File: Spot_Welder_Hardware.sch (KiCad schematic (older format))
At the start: 148 parts, among them J1 Mini USB, J2 Conn_01x03_Male, Q1 Q_NMOS_GSD, Q10 Q_NMOS_GDS, Q11 Q_NMOS_GDS, Q12 Q_NMOS_GDS, Q13 Q_NMOS_GDS, Q2 MBT3904, Q3 Q_NMOS_GDS, Q4 Q_NMOS_GDS, Q5 Q_NMOS_GDS, Q6 Q_NMOS_GDS, Q7 Q_NMOS_GDS, Q8 Q_NMOS_GDS, Q9 Q_NMOS_GDS, SW1 SW_Push, SW2 SW_SPDT, SW3 Lead Voltage Trigger, SW4 SW_Push, U1 OKI, U2 ATMEGA328P, U3 FAN3122TMXCT-ND, U4 FT232RL, U5 FAN3122TMXCT-ND, Y1 Crystal

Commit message: Updated shematic libraries
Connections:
- wire segments 326 -> 328
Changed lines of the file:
@@
 L MRDT_Connectors:AndersonPP Conn3
 U 1 1 5BB3DDFC
-P 5300 4200
-F 0 "Conn3" H 5506 4587 60  0000 C CNN
-F 1 "AndersonPP" H 5506 4481 60  0000 C CNN
-F 2 "MRDT_Connectors:Anderson_2_Horisontal_Side_by_Side" H 5150 3650 60  0001 C CNN
-F 3 "" H 5150 3650 60  0001 C CNN
-	1    5300 4200
+P 5250 4200
+F 0 "Conn3" H 5456 4587 60  0001 C CNN
+F 1 "AndersonPP" H 5456 4481 60  0001 C CNN
+F 2 "MRDT_Connectors:Anderson_2_Horisontal_Side_by_Side" H 5100 3650 60  0001 C CNN
+F 3 "" H 5100 3650 60  0001 C CNN
+	1    5250 4200
 	1    0    0    -1
 $EndComp
@@
 L MRDT_Connectors:AndersonPP Conn3
 U 2 1 5BB3DF96
-P 5300 3900
-F 0 "Conn3" H 5506 4287 60  0000 C CNN
-F 1 "AndersonPP" H 5506 4181 60  0000 C CNN
-F 2 "MRDT_Connectors:Anderson_2_Horisontal_Side_by_Side" H 5150 3350 60  0001 C CNN
-F 3 "" H 5150 3350 60  0001 C CNN
-	2    5300 3900
+P 5250 3900
+F 0 "Conn3" H 5456 4287 60  0000 C CNN
+F 1 "AndersonPP" H 5456 4181 60  0000 C CNN
+F 2 "MRDT_Connectors:Anderson_2_Horisontal_Side_by_Side" H 5100 3350 60  0001 C CNN
+F 3 "" H 5100 3350 60  0001 C CNN
+	2    5250 3900
 	1    0    0    -1
 $EndComp
@@
 	1    0    0    -1
 $EndComp
+Wire Wire Line
+	5650 3800 5700 3800
+Wire Wire Line
+	5650 4100 5700 4100
 $EndSCHEMATC

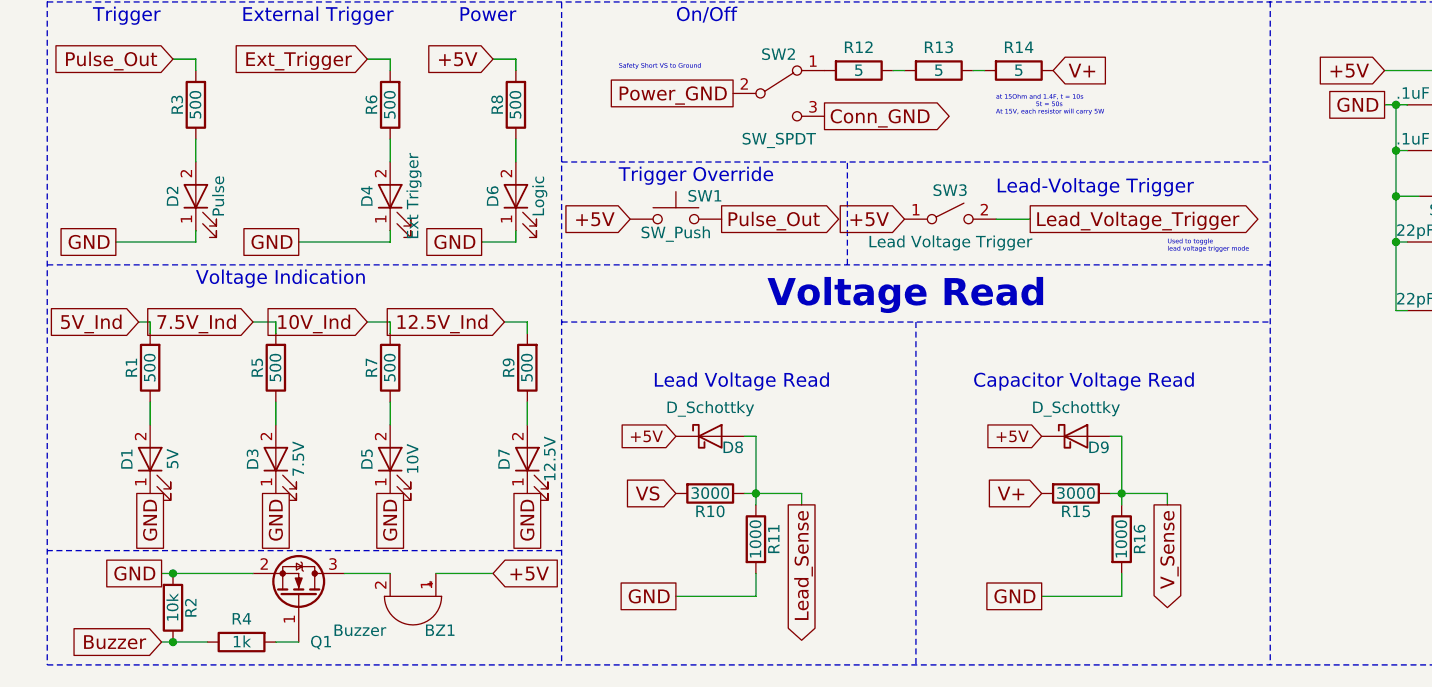
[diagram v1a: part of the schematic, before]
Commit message: Added pulldown Resistor to switches
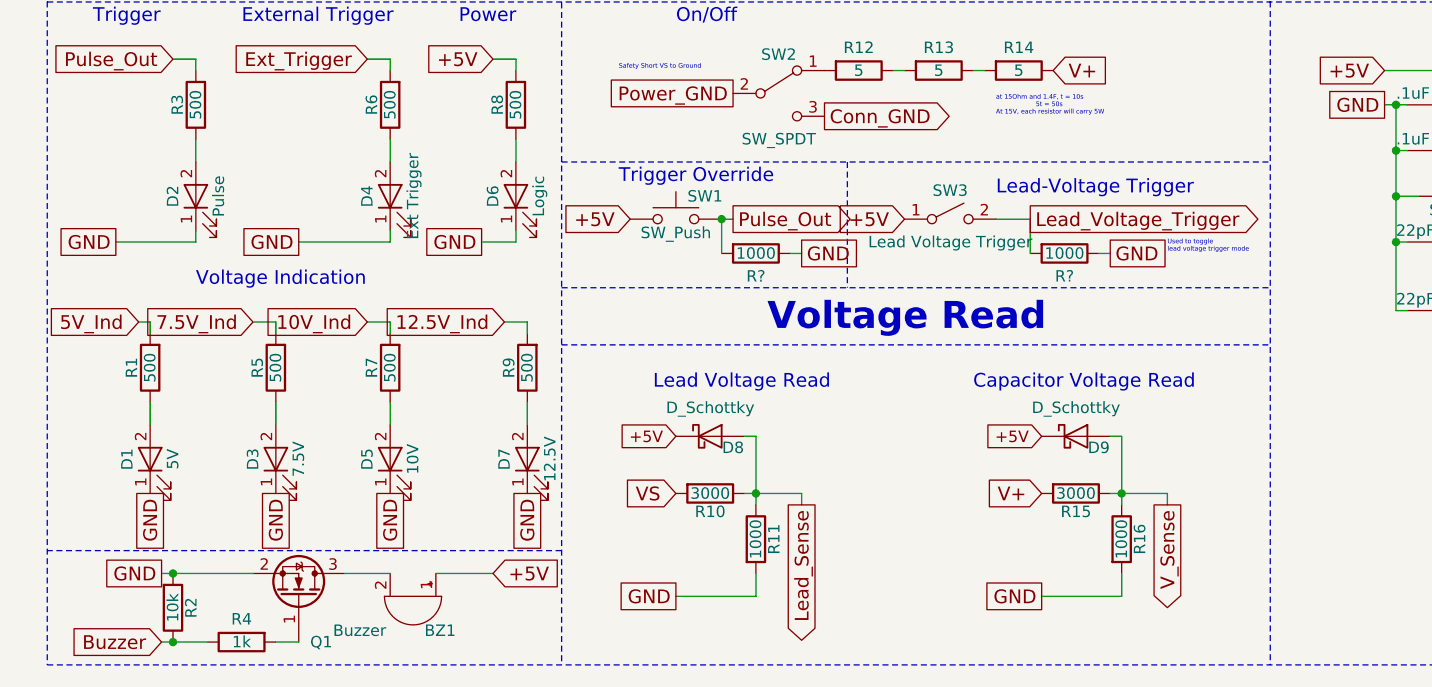
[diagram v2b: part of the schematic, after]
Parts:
- added R? (x2): 1000, symbol Device:R
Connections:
- wire segments 328 -> 333
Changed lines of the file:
@@
 Text GLabel 11250 4450 2    60   UnSpc ~ 0
 GND
-Text GLabel 4800 5750 2    60   Output ~ 0
+Text GLabel 4850 5750 2    60   Output ~ 0
 Pulse_Out
 Text GLabel 4400 5750 0    60   Input ~ 0
@@
 Text Notes 2050 4900 0    60   ~ 0
 Trigger
-Text Notes 5000 6150 0    118  ~ 24
+Text Notes 5000 6250 0    118  ~ 24
 Voltage Read
 $Comp
@@
 Wire Wire Line
 	12500 5850 12600 5850
-Wire Wire Line
-	6000 5750 6150 5750
 Wire Wire Line
 	2150 2700 2350 2700
@@
 	1850 7700 15300 7700
 Wire Notes Line
-	5650 6200 5650 7700
-Wire Notes Line
 	15300 7700 15300 1900
 Wire Notes Line
@@
 	3900 5850 3750 5850
 Wire Notes Line
-	1850 5950 7200 5950
-Wire Notes Line
-	4100 6200 7200 6200
-Wire Notes Line
 	4100 7200 1850 7200
 Text GLabel 10400 7100 2    60   Output ~ 0
@@
 Connection ~ 2400 7600
 Wire Notes Line
-	5350 5950 5350 5500
-Wire Notes Line
 	4100 5500 7200 5500
 $Comp
@@
 Wire Wire Line
 	5650 4100 5700 4100
+$Comp
+L Device:R R?
+U 1 1 5BFB6918
+P 4950 5900
+F 0 "R?" V 5050 5900 50  0000 C CNN
+F 1 "1000" V 4950 5900 50  0000 C CNN
+F 2 "" V 4880 5900 50  0001 C CNN
+F 3 "~" H 4950 5900 50  0001 C CNN
+	1    4950 5900
+	0    1    1    0
+$EndComp
+Wire Wire Line
+	4800 5900 4800 5750
+Text GLabel 5150 5900 2    60   UnSpc ~ 0
+GND
+Wire Wire Line
+	5100 5900 5150 5900
+Wire Wire Line
+	4800 5750 4850 5750
+Connection ~ 4800 5750
+Wire Notes Line
+	4100 6050 7200 6050
+Wire Notes Line
+	5350 5500 5350 6050
+Wire Notes Line
+	4100 6300 7200 6300
+$Comp
+L Device:R R?
+U 1 1 5C0EED75
+P 6300 5900
+F 0 "R?" V 6400 5900 50  0000 C CNN
+F 1 "1000" V 6300 5900 50  0000 C CNN
+F 2 "" V 6230 5900 50  0001 C CNN
+F 3 "~" H 6300 5900 50  0001 C CNN
+	1    6300 5900
+	0    1    1    0
+$EndComp
+Wire Wire Line
+	6150 5900 6150 5750
+Text GLabel 6500 5900 2    60   UnSpc ~ 0
+GND
+Wire Wire Line
+	6450 5900 6500 5900
+Wire Wire Line
+	6000 5750 6150 5750
 $EndSCHEMATC

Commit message: Fixed Layout
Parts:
- removed R?: 1000, symbol Device:R
- added R41: 1000, Resistors_SMD:R_0603_HandSoldering, symbol Device:R
- R42: renamed from R?; footprint (none) -> Resistors_SMD:R_0603_HandSoldering
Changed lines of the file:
@@
 Text Notes 8250 3750 0    60   ~ 0
 Logic Power
-Text Notes 4600 4900 0    60   ~ 0
+Text Notes 4900 4950 0    60   ~ 0
 On/Off
 Text Notes 3650 4900 0    60   ~ 0
@@
 Wire Wire Line
 	5650 4100 5700 4100
-$Comp
-L Device:R R?
-U 1 1 5BFB6918
+Wire Wire Line
+	4800 5900 4800 5750
+Text GLabel 5150 5900 2    60   UnSpc ~ 0
+GND
+Wire Wire Line
+	5100 5900 5150 5900
+Wire Wire Line
+	4800 5750 4850 5750
+Connection ~ 4800 5750
+Wire Notes Line
+	4100 6050 7200 6050
+Wire Notes Line
+	5350 5500 5350 6050
+Wire Notes Line
+	4100 6300 7200 6300
+$Comp
+L Device:R R42
+U 1 1 5C0EED75
+P 6300 5900
+F 0 "R42" V 6400 5900 50  0000 C CNN
+F 1 "1000" V 6300 5900 50  0000 C CNN
+F 2 "Resistors_SMD:R_0603_HandSoldering" V 6230 5900 50  0001 C CNN
+F 3 "~" H 6300 5900 50  0001 C CNN
+	1    6300 5900
+	0    1    1    0
+$EndComp
+Wire Wire Line
+	6150 5900 6150 5750
+Text GLabel 6500 5900 2    60   UnSpc ~ 0
+GND
+Wire Wire Line
+	6450 5900 6500 5900
+Wire Wire Line
+	6000 5750 6150 5750
+$Comp
+L Device:R R41
+U 1 1 5C17CF99
 P 4950 5900
-F 0 "R?" V 5050 5900 50  0000 C CNN
+F 0 "R41" V 5050 5900 50  0000 C CNN
 F 1 "1000" V 4950 5900 50  0000 C CNN
-F 2 "" V 4880 5900 50  0001 C CNN
+F 2 "Resistors_SMD:R_0603_HandSoldering" V 4880 5900 50  0001 C CNN
 F 3 "~" H 4950 5900 50  0001 C CNN
 	1    4950 5900
 	0    1    1    0
 $EndComp
-Wire Wire Line
-	4800 5900 4800 5750
-Text GLabel 5150 5900 2    60   UnSpc ~ 0
-GND
-Wire Wire Line
-	5100 5900 5150 5900
-Wire Wire Line
-	4800 5750 4850 5750
-Connection ~ 4800 5750
-Wire Notes Line
-	4100 6050 7200 6050
-Wire Notes Line
-	5350 5500 5350 6050
-Wire Notes Line
-	4100 6300 7200 6300
-$Comp
-L Device:R R?
-U 1 1 5C0EED75
-P 6300 5900
-F 0 "R?" V 6400 5900 50  0000 C CNN
-F 1 "1000" V 6300 5900 50  0000 C CNN
-F 2 "" V 6230 5900 50  0001 C CNN
-F 3 "~" H 6300 5900 50  0001 C CNN
-	1    6300 5900
-	0    1    1    0
-$EndComp
-Wire Wire Line
-	6150 5900 6150 5750
-Text GLabel 6500 5900 2    60   UnSpc ~ 0
-GND
-Wire Wire Line
-	6450 5900 6500 5900
-Wire Wire Line
-	6000 5750 6150 5750
 $EndSCHEMATC
